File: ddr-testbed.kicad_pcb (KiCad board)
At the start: 6 copper layers, 67.6 x 30 mm, 95 parts, among them J1 ddr3-sodimm-edge, U1 MT53E256M16D1

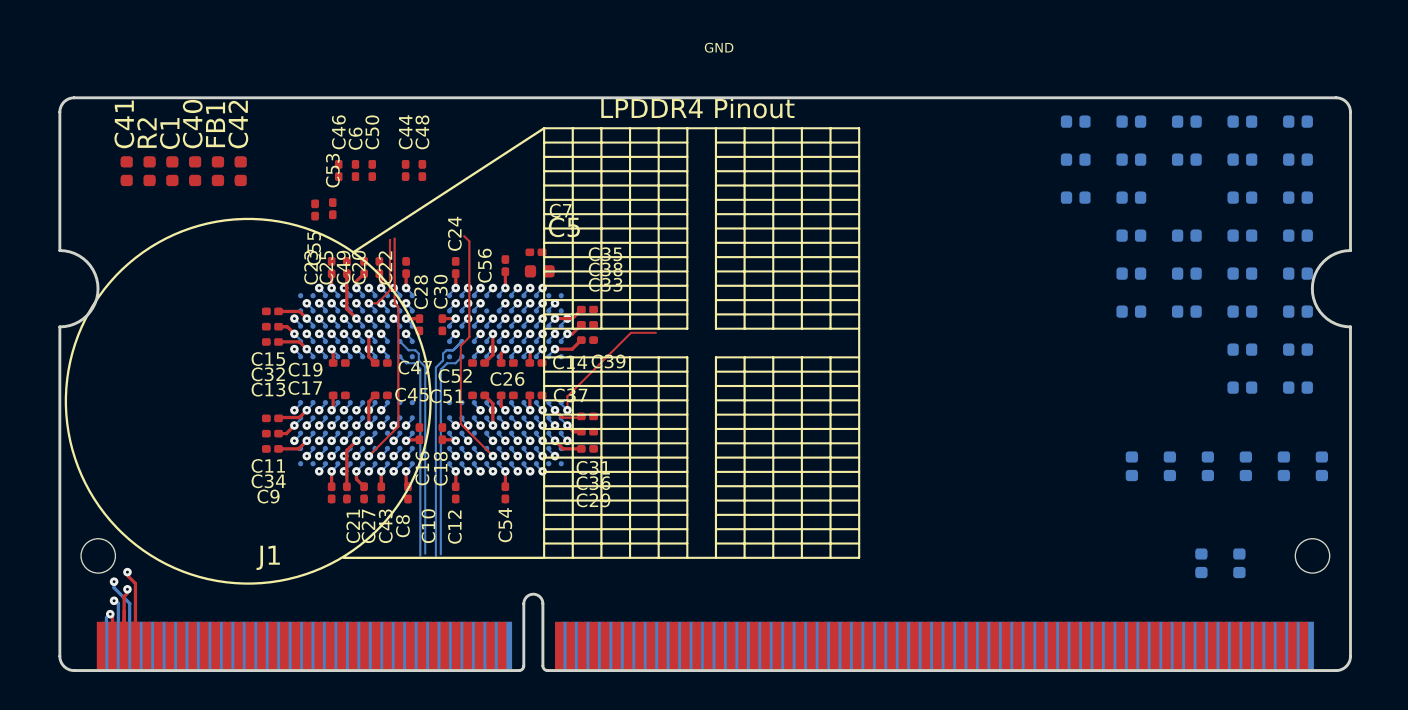
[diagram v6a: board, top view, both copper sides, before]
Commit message: Passive components update, edge connector routing wip
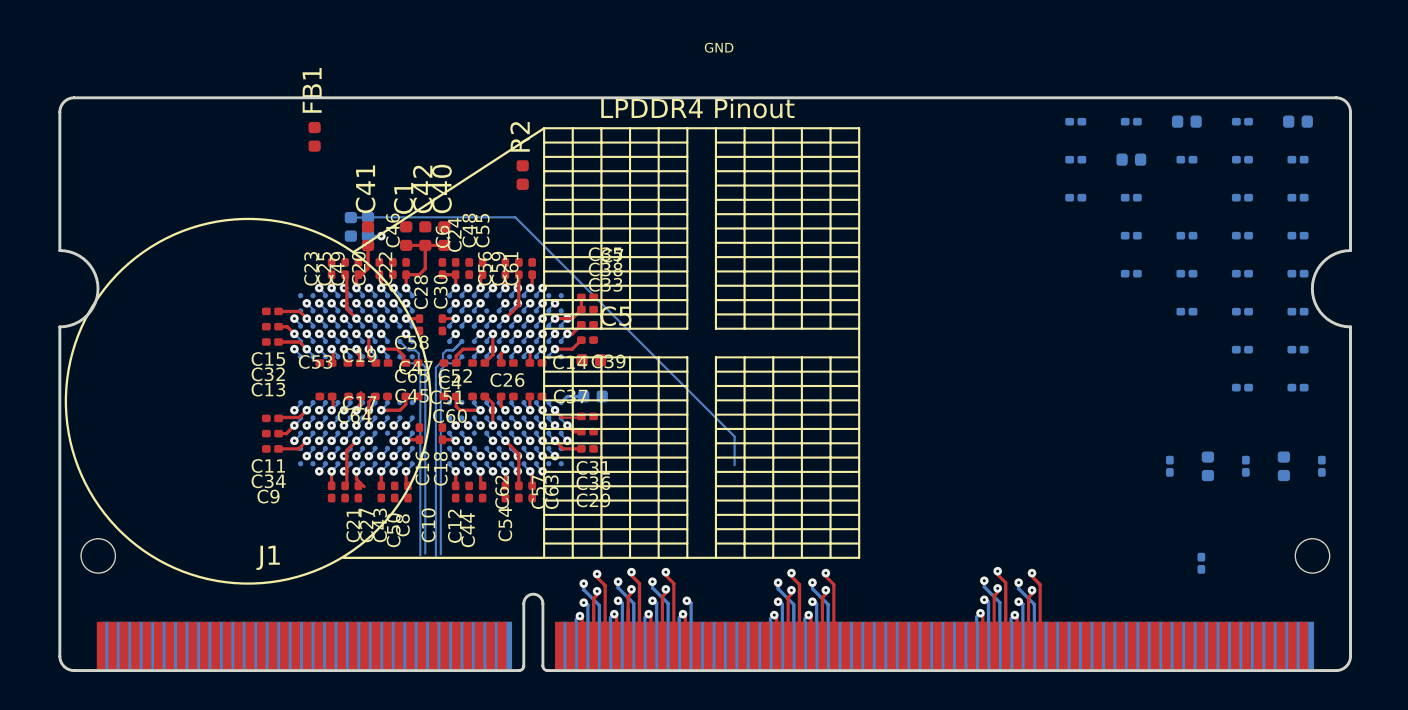
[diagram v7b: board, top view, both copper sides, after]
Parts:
- added C4: C_100n_0201, antmicro-footprints:0201-res, F.Cu at (121.5, 85.2)
- added C57: C_100n_0201, antmicro-footprints:0201-res, F.Cu at (125.1, 91.9)
- added C58: C_100n_0201, antmicro-footprints:0201-res, F.Cu at (119.5, 85.2)
- added C59: C_100n_0201, antmicro-footprints:0201-res, F.Cu at (125.1, 80.2)
- added C60: C_100n_0201, antmicro-footprints:0201-res, F.Cu at (121.5, 86.9)
- added C61: C_100n_0201, antmicro-footprints:0201-res, F.Cu at (125.8, 80.2)
- added C62: C_100n_0201, antmicro-footprints:0201-res, F.Cu at (123.2, 91.9)
- added C63: C_100n_0201, antmicro-footprints:0201-res, F.Cu at (125.8, 91.9)
- added C64: C_100n_0201, antmicro-footprints:0201-res, F.Cu at (116.5, 86.9)
- added C65: C_100n_0201, antmicro-footprints:0201-res, F.Cu at (119.5, 86.9)
- R11, R12, R20, R21, R22, R23, R24, R25, R26, R27, R28, R29, R30, R31, R32, R33, R34, R4, R5, R6, R7, R8, R9: footprint antmicro-footprints:0402-res -> antmicro-footprints:0201-res
- R13, R14, R15, R16, R17, R18, R19: value R_40R2_0402 -> R_40R2_0201; footprint antmicro-footprints:0402-res -> antmicro-footprints:0201-res
- moved R36 48.9 mm to (117.2, 78.0)
- moved R35 42.8 mm to (116.3, 78.0)
- moved R1 28.5 mm to (129.0, 86.9), turned to 0 degrees
- moved R2 19.5 mm to (125.3, 75.3)
- moved C44 17.2 mm to (122.5, 91.9), turned to 270 degrees
- moved C50 16.9 mm to (118.6, 91.9), turned to 270 degrees
- moved C40 13.5 mm to (121.2, 78.5)
- moved C41 13.1 mm to (117.2, 78.5)
- moved C1 12.7 mm to (119.2, 78.5)
- moved C42 10.2 mm to (120.2, 78.5)
- moved C55 9.29 mm to (123.2, 80.2), turned to 90 degrees
- moved C53 8.16 mm to (116.5, 85.2), turned to 180 degrees
- moved C6 6.87 mm to (121.1, 80.2)
- moved C46 5.87 mm to (118.5, 80.2)
- moved C48 5.70 mm to (122.5, 80.2)
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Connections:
- C10 pad 1: Net-(C10-Pad1) -> VDD2
- C10 pad 2: Net-(C10-Pad2) -> GND
- C11 pad 1: Net-(C11-Pad1) -> VDDQ
- C11 pad 2: Net-(C11-Pad2) -> GND
- C12 pad 1: Net-(C12-Pad1) -> VDD2
- C12 pad 2: Net-(C12-Pad2) -> GND
- C13 pad 1: Net-(C13-Pad1) -> VDDQ
- C13 pad 2: Net-(C13-Pad2) -> GND
- C14 pad 1: Net-(C14-Pad1) -> VDD2
- C14 pad 2: Net-(C14-Pad2) -> GND
- C15 pad 1: Net-(C15-Pad1) -> VDDQ
- C15 pad 2: Net-(C15-Pad2) -> GND
- C16 pad 1: Net-(C16-Pad1) -> VDD2
- C16 pad 2: Net-(C16-Pad2) -> GND
- C17 pad 1: Net-(C17-Pad1) -> VDDQ
- C17 pad 2: Net-(C17-Pad2) -> GND
- C18 pad 1: Net-(C18-Pad1) -> VDD2
- C18 pad 2: Net-(C18-Pad2) -> GND
- C19 pad 1: Net-(C19-Pad1) -> VDDQ
- C19 pad 2: Net-(C19-Pad2) -> GND
- C20 pad 1: Net-(C20-Pad1) -> VDD2
- C20 pad 2: Net-(C20-Pad2) -> GND
- C21 pad 1: Net-(C21-Pad1) -> VDDQ
- C21 pad 2: Net-(C21-Pad2) -> GND
- C22 pad 1: Net-(C22-Pad1) -> VDD2
- C22 pad 2: Net-(C22-Pad2) -> GND
- C23 pad 1: Net-(C23-Pad1) -> VDDQ
- C23 pad 2: Net-(C23-Pad2) -> GND
- C24 pad 1: Net-(C24-Pad1) -> VDD2
- C24 pad 2: Net-(C24-Pad2) -> GND
- C25 pad 1: Net-(C25-Pad1) -> VDDQ
- C25 pad 2: Net-(C25-Pad2) -> GND
- C26 pad 1: Net-(C26-Pad1) -> VDD2
- C26 pad 2: Net-(C26-Pad2) -> GND
- C27 pad 1: Net-(C27-Pad1) -> VDDQ
- C27 pad 2: Net-(C27-Pad2) -> GND
- C28 pad 1: Net-(C28-Pad1) -> VDD2
- C28 pad 2: Net-(C28-Pad2) -> GND
- C29 pad 1: Net-(C29-Pad1) -> VDDQ
- C29 pad 2: Net-(C29-Pad2) -> GND
- C30 pad 1: Net-(C30-Pad1) -> VDD2
- C30 pad 2: Net-(C30-Pad2) -> GND
- C31 pad 1: Net-(C31-Pad1) -> VDDQ
- C31 pad 2: Net-(C31-Pad2) -> GND
- C32 pad 1: Net-(C32-Pad1) -> VDD2
- C32 pad 2: Net-(C32-Pad2) -> GND
- C33 pad 1: Net-(C33-Pad1) -> VDDQ
- C33 pad 2: Net-(C33-Pad2) -> GND
- C34 pad 1: Net-(C34-Pad1) -> VDD2
- C34 pad 2: Net-(C34-Pad2) -> GND
- C35 pad 1: Net-(C35-Pad1) -> VDDQ
- C35 pad 2: Net-(C35-Pad2) -> GND
- C36 pad 1: Net-(C36-Pad1) -> VDD2
- C36 pad 2: Net-(C36-Pad2) -> GND
- C37 pad 1: Net-(C37-Pad1) -> VDDQ
- C37 pad 2: Net-(C37-Pad2) -> GND
- C43 pad 1: Net-(C43-Pad1) -> VDD1
- C43 pad 2: Net-(C43-Pad2) -> GND
- C44 pad 1: Net-(C44-Pad1) -> VDD2
- C44 pad 2: Net-(C44-Pad2) -> GND
- C45 pad 1: Net-(C45-Pad1) -> VDD1
- C45 pad 2: Net-(C45-Pad2) -> GND
- C46 pad 1: Net-(C46-Pad1) -> VDD2
- C46 pad 2: Net-(C46-Pad2) -> GND
- C47 pad 1: Net-(C47-Pad1) -> VDD1
- C47 pad 2: Net-(C47-Pad2) -> GND
- C48 pad 1: Net-(C48-Pad1) -> VDD2
- C48 pad 2: Net-(C48-Pad2) -> GND
- C49 pad 1: Net-(C49-Pad1) -> VDD1
- C49 pad 2: Net-(C49-Pad2) -> GND
- C50 pad 1: Net-(C50-Pad1) -> VDD2
- C50 pad 2: Net-(C50-Pad2) -> GND
- C51 pad 1: Net-(C51-Pad1) -> VDD1
- C51 pad 2: Net-(C51-Pad2) -> GND
- C52 pad 1: Net-(C52-Pad1) -> VDD1
- C52 pad 2: Net-(C52-Pad2) -> GND
- C53 pad 1: Net-(C53-Pad1) -> VDD2
- C53 pad 2: Net-(C53-Pad2) -> GND
- C54 pad 1: Net-(C54-Pad1) -> VDD1
- C54 pad 2: Net-(C54-Pad2) -> GND
- C6 pad 1: Net-(C6-Pad1) -> VDD2
- C6 pad 2: Net-(C6-Pad2) -> GND
- C7 pad 1: Net-(C7-Pad1) -> VDDQ
- C7 pad 2: Net-(C7-Pad2) -> GND
- C8 pad 1: Net-(C8-Pad1) -> VDD2
- C8 pad 2: Net-(C8-Pad2) -> GND
- C9 pad 1: Net-(C9-Pad1) -> VDDQ
- C9 pad 2: Net-(C9-Pad2) -> GND
- J1 pad 86: Net-(J1-Pad86) -> /CS_1_N
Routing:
- net /RESET_CONN_N: track 0.00 -> 26.4 mm
- net GND: track 31.0 -> 56.0 mm, vias 58 -> 66
- net VDD2: track 25.8 -> 41.5 mm
- net /ODT0_A: track 13.0 -> 0.53 mm
- net /ODT0_B: track 12.7 -> 0.53 mm
- net VDDQ: track 33.9 -> 41.6 mm
- net Net-(R1-Pad1): track 7.26 -> 1.39 mm, vias 1 -> 0
- net /CA1_B: track 13.9 -> 19.7 mm, vias 1 -> 2
- net Net-(J1-Pad5): track 5.86 -> 0.00 mm, vias 1 -> 0
- net /DQS2_N: track 5.44 -> 9.78 mm, vias 1 -> 2
- net /DQ15: track 11.4 -> 15.7 mm, vias 1 -> 2
- net /CA2_B: track 17.1 -> 21.5 mm, vias 1 -> 2
- net Net-(J1-Pad7): track 4.34 -> 0.00 mm, vias 1 -> 0
- net /DQ20: track 6.74 -> 11.1 mm, vias 1 -> 2
- net /DQ13: track 12.6 -> 16.9 mm, vias 1 -> 2
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
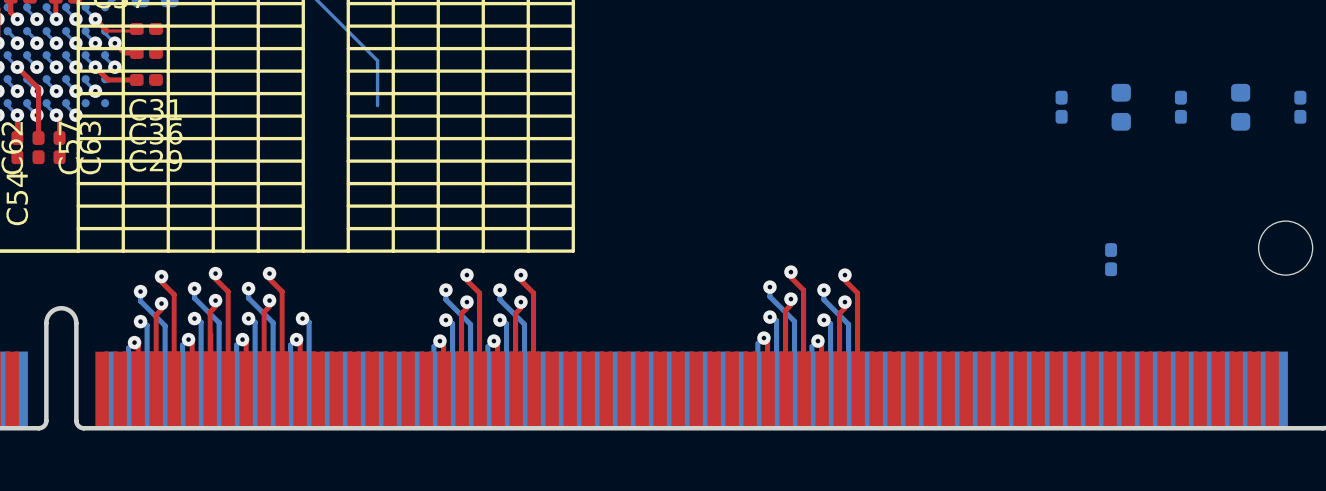
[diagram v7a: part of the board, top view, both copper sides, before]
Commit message: Added edge connector escape
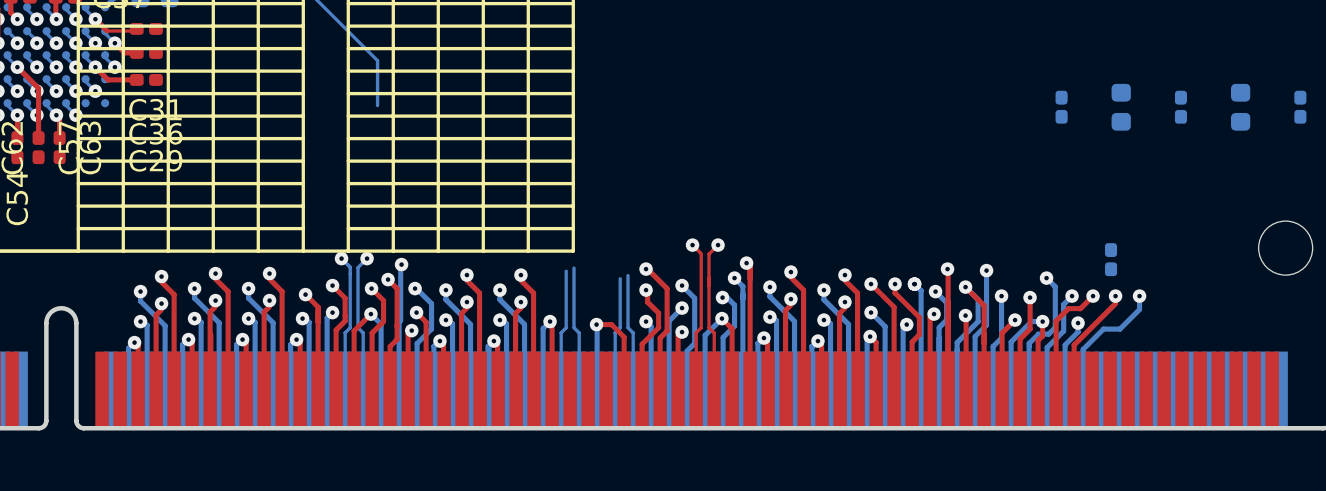
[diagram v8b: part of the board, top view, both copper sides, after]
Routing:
- net GND: track 56.0 -> 113.4 mm, vias 66 -> 80
- net /CA0_A: track 11.3 -> 18.5 mm, vias 1 -> 2
- net /DQ11: track 18.3 -> 24.1 mm, vias 1 -> 2
- net /DQS0_P: track 5.38 -> 10.6 mm, vias 1 -> 2
- net /DQ01: track 4.04 -> 9.24 mm, vias 1 -> 2
- net /RESET_CONN_N: track 26.4 -> 31.5 mm, vias 0 -> 1
- net /DM0_N: track 5.57 -> 10.7 mm, vias 1 -> 2
- net /DQ04: track 7.25 -> 12.3 mm, vias 1 -> 2
- net /DQ00: track 4.17 -> 9.17 mm, vias 1 -> 2
- net /DQS0_N: track 5.38 -> 10.4 mm, vias 1 -> 2
- net /ODT0: track 0.00 -> 4.97 mm, vias 0 -> 1
- net /DQ29: track 13.1 -> 18.1 mm, vias 1 -> 2
- net /CA4_A: track 17.4 -> 22.3 mm, vias 1 -> 2
- net /DQ03: track 3.45 -> 8.32 mm, vias 1 -> 2
- net /DQ22: track 5.98 -> 10.8 mm, vias 1 -> 2
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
